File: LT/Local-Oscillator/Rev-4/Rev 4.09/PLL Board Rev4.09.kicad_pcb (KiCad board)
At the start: 2 copper layers, 109.2 x 45.7 mm, 69 parts, among them J1 Conn_01x02_Male, J13 Conn_01x02_Male, J14 Conn_01x02_Male, J15 Conn_01x02_Male, J16 Conn_01x02_Male, J17 Conn_01x02_Male, J18 Conn_Coaxial, J2 Conn_Coaxial, J20 Conn_01x02_Male, J3 Conn_Coaxial, J4 Conn_01x04_Male, J5 Conn_01x02_Male, J7 Conn_01x02_Male, J8 Conn_01x02_Male, Q1 2N5486 JFET, Q2 2N5486 JFET, U1 LMX231X, U2 L7808

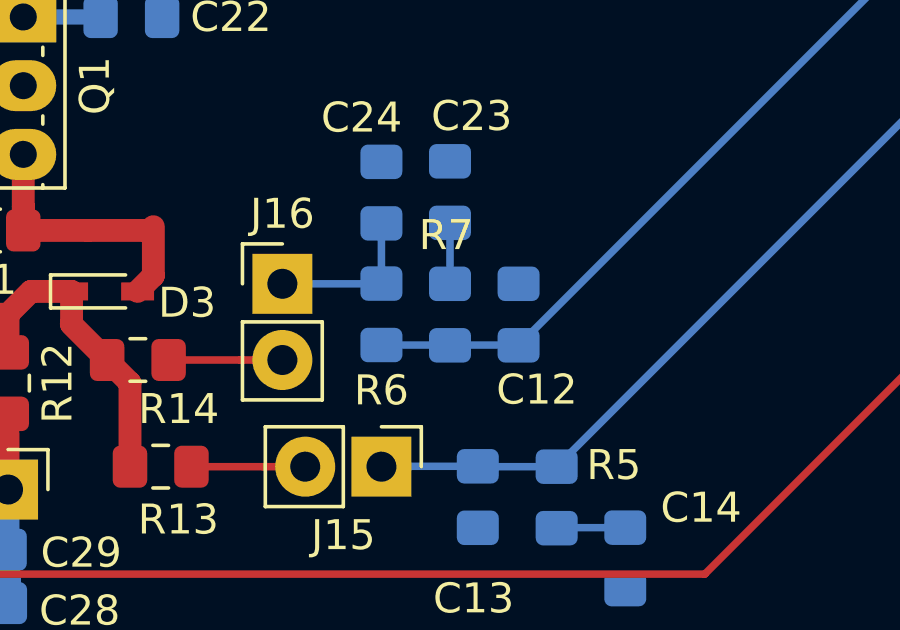
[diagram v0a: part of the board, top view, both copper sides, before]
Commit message: Finished PLL Revisions on KiCad
The KiCad files for the PLL have been uploaded to github and the integration to the "Real Resistor" symbol has begun
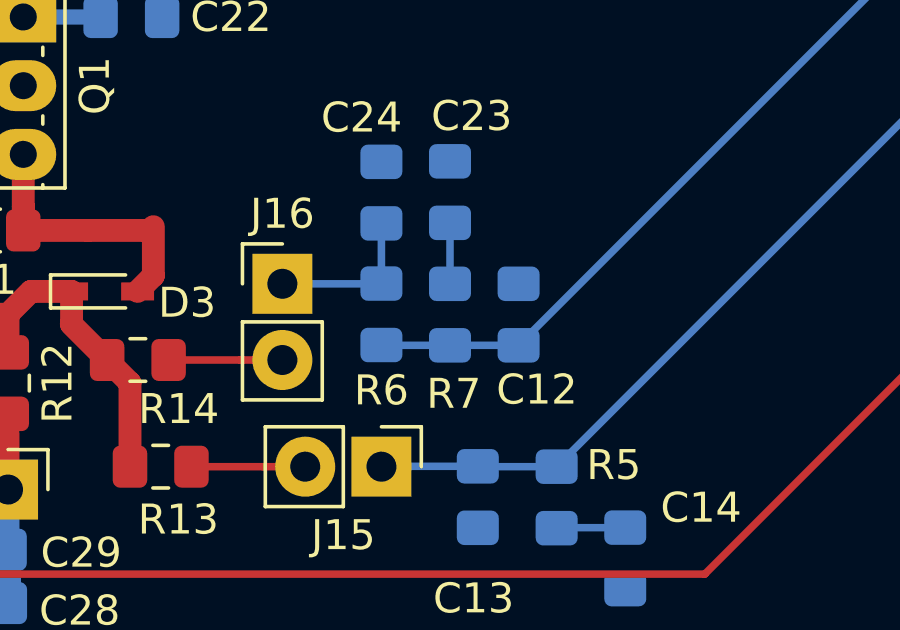
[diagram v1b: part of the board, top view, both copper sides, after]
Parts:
- C19: value TZB4Z100BA10R00 -> SGC35060
- D3, D4: value ??? -> 1SV304
- turned R7 to 90 degrees
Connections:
- R7 pad 1: Net-(C23-Pad1) -> Net-(C12-Pad2)
- R7 pad 2: Net-(C12-Pad2) -> Net-(C23-Pad1)
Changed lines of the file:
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@@
     (thickness 1.6)
     (drawings 4)
-    (tracks 248)
+    (tracks 247)
     (zones 0)
     (modules 69)
@@
       (effects (font (size 1 1) (thickness 0.15)))
     )
-    (fp_text value "TZB4Z100BA10R00 " (at 0 3.25 270) (layer F.Fab)
+    (fp_text value SGC35060 (at 0 3.25 270) (layer F.Fab)
       (effects (font (size 1 1) (thickness 0.15)))
     )
@@
   )
   (module Resistor_SMD:R_0805_2012Metric_Pad1.15x1.40mm_HandSolder (layer B.Cu)
-    (at 122.428 102.625 270)
+    (at 122.428 102.625 90)
     (descr "Resistor SMD 0805 (2012 Metric), square (rectangular) end terminal, IPC_7351 nominal with elongated pad for handsoldering. (Body size source: https://docs.google.com/spreadsheets/d/1BsfQQcO9C6DZCsRaXUlFlo91Tg2WpOkGARC1WS5S8t0/edit?usp=sharing), generated with kicad-footprint-generator")
     (tags "resistor handsolder")
@@
       (effects (font (size 0.5 0.5) (thickness 0.08)) (justify mirror))
     )
-    (pad 1 smd roundrect (at -1.025 0 270) (size 1.15 1.4) (layers B.Cu B.Paste B.Mask) (roundrect_rratio 0.217391)
-      (net 35 "Net-(C23-Pad1)"))
-    (pad 2 smd roundrect (at 1.025 0 270) (size 1.15 1.4) (layers B.Cu B.Paste B.Mask) (roundrect_rratio 0.217391)
+    (pad 1 smd roundrect (at -1.025 0 90) (size 1.15 1.4) (layers B.Cu B.Paste B.Mask) (roundrect_rratio 0.217391)
       (net 6 "Net-(C12-Pad2)"))
+    (pad 2 smd roundrect (at 1.025 0 90) (size 1.15 1.4) (layers B.Cu B.Paste B.Mask) (roundrect_rratio 0.217391)
+      (net 35 "Net-(C23-Pad1)"))
     (model ${KISYS3DMOD}/Resistor_SMD.3dshapes/R_0805_2012Metric.wrl
       (at (xyz 0 0 0))
@@
       (effects (font (size 1 1) (thickness 0.15)))
     )
-    (fp_text value ??? (at 0 1.6) (layer F.Fab)
+    (fp_text value 1SV304 (at 0 1.6) (layer F.Fab)
       (effects (font (size 1 1) (thickness 0.15)))
     )
@@
       (effects (font (size 1 1) (thickness 0.15)))
     )
-    (fp_text value ??? (at 0 1.6 270) (layer F.Fab)
+    (fp_text value 1SV304 (at 0 1.6 270) (layer F.Fab)
       (effects (font (size 1 1) (thickness 0.15)))
     )
@@
   (segment (start 141.478 90.424) (end 137.94 90.424) (width 0.25) (layer B.Cu) (net 6) (status 10))
   (segment (start 120.151 103.65) (end 120.142 103.641) (width 0.25) (layer B.Cu) (net 6) (status 30))
-  (segment (start 124.705 103.641) (end 124.714 103.65) (width 0.25) (layer B.Cu) (net 6))
-  (segment (start 120.142 103.641) (end 124.705 103.641) (width 0.25) (layer B.Cu) (net 6))
+  (segment (start 124.714 103.65) (end 120.151 103.65) (width 0.25) (layer B.Cu) (net 6) (status 30))
   (segment (start 105.918 94.996) (end 105.664 95.25) (width 0.508) (layer F.Cu) (net 7) (status 30))
   (segment (start 108.204 94.996) (end 105.918 94.996) (width 0.508) (layer F.Cu) (net 7) (status 30))
@@
   (segment (start 86.5552 97.1042) (end 86.5124 97.0614) (width 0.25) (layer F.Cu) (net 34) (status 30))
   (segment (start 89.154 97.1042) (end 86.5552 97.1042) (width 0.508) (layer F.Cu) (net 34) (status 30))
-  (segment (start 122.428 99.568) (end 122.428 101.6) (width 0.25) (layer B.Cu) (net 35))
+  (segment (start 122.428 101.6) (end 122.428 99.568) (width 0.25) (layer B.Cu) (net 35) (status 30))
   (segment (start 120.142 101.591) (end 120.142 99.586) (width 0.25) (layer B.Cu) (net 36) (status 30))
   (segment (start 120.133 101.6) (end 120.142 101.591) (width 0.25) (layer B.Cu) (net 36) (status 30))

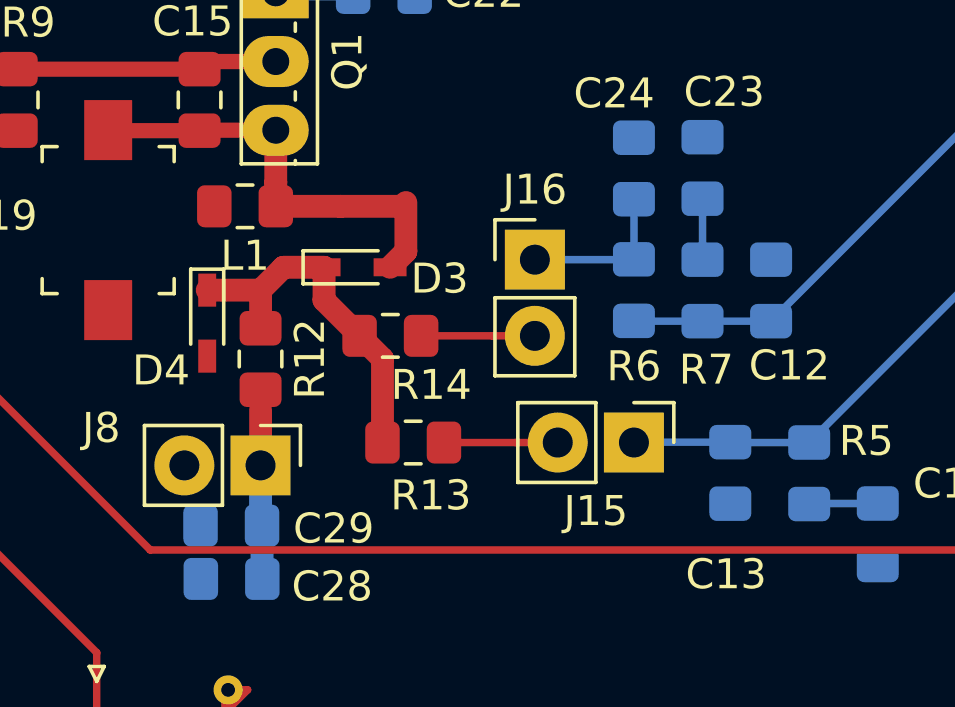
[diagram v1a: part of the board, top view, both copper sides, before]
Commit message: Finished PLL Resistor Symbols
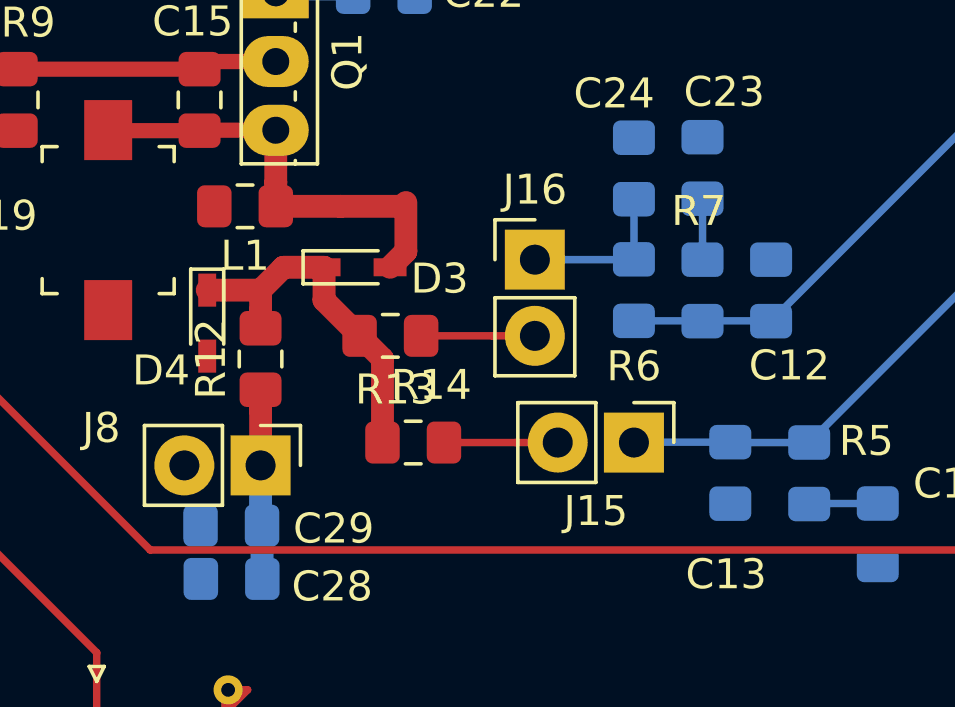
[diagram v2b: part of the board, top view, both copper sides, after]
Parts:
- R13, R14: value 0k -> 0
- turned R12 to 90 degrees
- turned R13 to 180 degrees
- turned R7 to 270 degrees
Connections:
- R12 pad 1: Net-(D3-Pad1) -> Net-(C28-Pad2)
- R12 pad 2: Net-(C28-Pad2) -> Net-(D3-Pad1)
- R13 pad 1: Net-(D3-Pad1) -> Net-(J15-Pad2)
- R13 pad 2: Net-(J15-Pad2) -> Net-(D3-Pad1)
- R7 pad 1: Net-(C12-Pad2) -> Net-(C23-Pad1)
- R7 pad 2: Net-(C23-Pad1) -> Net-(C12-Pad2)
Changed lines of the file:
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@@
     (thickness 1.6)
     (drawings 4)
-    (tracks 247)
+    (tracks 249)
     (zones 0)
     (modules 69)
@@
       (effects (font (size 1 1) (thickness 0.15)))
     )
-    (fp_text value 0k (at 0 1.65 180) (layer F.Fab)
+    (fp_text value 0 (at 0 1.65 180) (layer F.Fab)
       (effects (font (size 1 1) (thickness 0.15)))
     )
@@
   )
   (module Resistor_SMD:R_0805_2012Metric_Pad1.15x1.40mm_HandSolder (layer F.Cu)
-    (at 112.785 107.696)
+    (at 112.785 107.696 180)
     (descr "Resistor SMD 0805 (2012 Metric), square (rectangular) end terminal, IPC_7351 nominal with elongated pad for handsoldering. (Body size source: https://docs.google.com/spreadsheets/d/1BsfQQcO9C6DZCsRaXUlFlo91Tg2WpOkGARC1WS5S8t0/edit?usp=sharing), generated with kicad-footprint-generator")
     (tags "resistor handsolder")
@@
       (effects (font (size 1 1) (thickness 0.15)))
     )
-    (fp_text value 0k (at 0 1.65) (layer F.Fab)
+    (fp_text value 0 (at 0 1.65) (layer F.Fab)
       (effects (font (size 1 1) (thickness 0.15)))
     )
@@
       (effects (font (size 0.5 0.5) (thickness 0.08)))
     )
-    (pad 1 smd roundrect (at -1.025 0) (size 1.15 1.4) (layers F.Cu F.Paste F.Mask) (roundrect_rratio 0.217391)
-      (net 13 "Net-(D3-Pad1)"))
-    (pad 2 smd roundrect (at 1.025 0) (size 1.15 1.4) (layers F.Cu F.Paste F.Mask) (roundrect_rratio 0.217391)
+    (pad 1 smd roundrect (at -1.025 0 180) (size 1.15 1.4) (layers F.Cu F.Paste F.Mask) (roundrect_rratio 0.217391)
       (net 37 "Net-(J15-Pad2)"))
+    (pad 2 smd roundrect (at 1.025 0 180) (size 1.15 1.4) (layers F.Cu F.Paste F.Mask) (roundrect_rratio 0.217391)
+      (net 13 "Net-(D3-Pad1)"))
     (model ${KISYS3DMOD}/Resistor_SMD.3dshapes/R_0805_2012Metric.wrl
       (at (xyz 0 0 0))
@@
   )
   (module Resistor_SMD:R_0805_2012Metric_Pad1.15x1.40mm_HandSolder (layer F.Cu)
-    (at 107.696 104.911 270)
+    (at 107.696 104.911 90)
     (descr "Resistor SMD 0805 (2012 Metric), square (rectangular) end terminal, IPC_7351 nominal with elongated pad for handsoldering. (Body size source: https://docs.google.com/spreadsheets/d/1BsfQQcO9C6DZCsRaXUlFlo91Tg2WpOkGARC1WS5S8t0/edit?usp=sharing), generated with kicad-footprint-generator")
     (tags "resistor handsolder")
@@
       (effects (font (size 0.5 0.5) (thickness 0.08)))
     )
-    (pad 1 smd roundrect (at -1.025 0 270) (size 1.15 1.4) (layers F.Cu F.Paste F.Mask) (roundrect_rratio 0.217391)
-      (net 13 "Net-(D3-Pad1)"))
-    (pad 2 smd roundrect (at 1.025 0 270) (size 1.15 1.4) (layers F.Cu F.Paste F.Mask) (roundrect_rratio 0.217391)
+    (pad 1 smd roundrect (at -1.025 0 90) (size 1.15 1.4) (layers F.Cu F.Paste F.Mask) (roundrect_rratio 0.217391)
       (net 39 "Net-(C28-Pad2)"))
+    (pad 2 smd roundrect (at 1.025 0 90) (size 1.15 1.4) (layers F.Cu F.Paste F.Mask) (roundrect_rratio 0.217391)
+      (net 13 "Net-(D3-Pad1)"))
     (model ${KISYS3DMOD}/Resistor_SMD.3dshapes/R_0805_2012Metric.wrl
       (at (xyz 0 0 0))
@@
   )
   (module Resistor_SMD:R_0805_2012Metric_Pad1.15x1.40mm_HandSolder (layer B.Cu)
-    (at 122.428 102.625 90)
+    (at 122.428 102.625 270)
     (descr "Resistor SMD 0805 (2012 Metric), square (rectangular) end terminal, IPC_7351 nominal with elongated pad for handsoldering. (Body size source: https://docs.google.com/spreadsheets/d/1BsfQQcO9C6DZCsRaXUlFlo91Tg2WpOkGARC1WS5S8t0/edit?usp=sharing), generated with kicad-footprint-generator")
     (tags "resistor handsolder")
@@
       (effects (font (size 0.5 0.5) (thickness 0.08)) (justify mirror))
     )
-    (pad 1 smd roundrect (at -1.025 0 90) (size 1.15 1.4) (layers B.Cu B.Paste B.Mask) (roundrect_rratio 0.217391)
-      (net 6 "Net-(C12-Pad2)"))
-    (pad 2 smd roundrect (at 1.025 0 90) (size 1.15 1.4) (layers B.Cu B.Paste B.Mask) (roundrect_rratio 0.217391)
+    (pad 1 smd roundrect (at -1.025 0 270) (size 1.15 1.4) (layers B.Cu B.Paste B.Mask) (roundrect_rratio 0.217391)
       (net 35 "Net-(C23-Pad1)"))
+    (pad 2 smd roundrect (at 1.025 0 270) (size 1.15 1.4) (layers B.Cu B.Paste B.Mask) (roundrect_rratio 0.217391)
+      (net 6 "Net-(C12-Pad2)"))
     (model ${KISYS3DMOD}/Resistor_SMD.3dshapes/R_0805_2012Metric.wrl
       (at (xyz 0 0 0))
@@
   (segment (start 141.478 90.424) (end 137.94 90.424) (width 0.25) (layer B.Cu) (net 6) (status 10))
   (segment (start 120.151 103.65) (end 120.142 103.641) (width 0.25) (layer B.Cu) (net 6) (status 30))
-  (segment (start 124.714 103.65) (end 120.151 103.65) (width 0.25) (layer B.Cu) (net 6) (status 30))
+  (segment (start 124.705 103.641) (end 124.714 103.65) (width 0.25) (layer B.Cu) (net 6))
+  (segment (start 120.142 103.641) (end 124.705 103.641) (width 0.25) (layer B.Cu) (net 6))
   (segment (start 105.918 94.996) (end 105.664 95.25) (width 0.508) (layer F.Cu) (net 7) (status 30))
   (segment (start 108.204 94.996) (end 105.918 94.996) (width 0.508) (layer F.Cu) (net 7) (status 30))
@@
   (segment (start 184.8358 87.9856) (end 184.8358 93.6498) (width 0.762) (layer F.Cu) (net 12) (status 30))
   (segment (start 111.76 104.902) (end 110.998 104.14) (width 0.762) (layer F.Cu) (net 13) (status 20))
-  (segment (start 111.76 107.696) (end 111.76 104.902) (width 0.762) (layer F.Cu) (net 13) (status 10))
   (segment (start 110.064 101.854) (end 109.814 101.854) (width 0.25) (layer F.Cu) (net 13) (status 30))
   (segment (start 105.918 102.366) (end 105.918 102.616) (width 0.25) (layer F.Cu) (net 13) (status 30))
   (segment (start 109.728 101.854) (end 109.814 101.854) (width 0.25) (layer F.Cu) (net 13) (status 30))
   (segment (start 106.468 102.616) (end 105.918 102.616) (width 0.762) (layer F.Cu) (net 13) (status 20))
-  (segment (start 107.696 103.886) (end 107.696 102.616) (width 0.762) (layer F.Cu) (net 13) (status 10))
   (segment (start 107.696 102.616) (end 106.468 102.616) (width 0.762) (layer F.Cu) (net 13))
   (segment (start 108.458 101.854) (end 109.814 101.854) (width 0.762) (layer F.Cu) (net 13) (status 20))
@@
   (segment (start 109.814 102.9364) (end 109.814 101.854) (width 0.762) (layer F.Cu) (net 13) (status 20))
   (segment (start 109.8042 102.9462) (end 109.814 102.9364) (width 0.25) (layer F.Cu) (net 13))
+  (segment (start 111.76 104.902) (end 111.76 107.696) (width 0.762) (layer F.Cu) (net 13))
+  (segment (start 107.696 103.311) (end 107.696 102.616) (width 0.762) (layer F.Cu) (net 13))
+  (segment (start 107.696 103.886) (end 107.696 103.311) (width 0.762) (layer F.Cu) (net 13))
   (segment (start 114.663787 87.376) (end 112.268 87.376) (width 0.508) (layer B.Cu) (net 14) (status 20))
   (segment (start 116.078 87.376) (end 114.663787 87.376) (width 0.508) (layer B.Cu) (net 14) (status 10))
@@
   (segment (start 86.5552 97.1042) (end 86.5124 97.0614) (width 0.25) (layer F.Cu) (net 34) (status 30))
   (segment (start 89.154 97.1042) (end 86.5552 97.1042) (width 0.508) (layer F.Cu) (net 34) (status 30))
-  (segment (start 122.428 101.6) (end 122.428 99.568) (width 0.25) (layer B.Cu) (net 35) (status 30))
+  (segment (start 122.428 99.568) (end 122.428 101.6) (width 0.25) (layer B.Cu) (net 35))
   (segment (start 120.142 101.591) (end 120.142 99.586) (width 0.25) (layer B.Cu) (net 36) (status 30))
   (segment (start 120.133 101.6) (end 120.142 101.591) (width 0.25) (layer B.Cu) (net 36) (status 30))
   (segment (start 116.84 101.6) (end 120.133 101.6) (width 0.25) (layer B.Cu) (net 36) (status 30))
-  (segment (start 116.187787 107.696) (end 113.81 107.696) (width 0.25) (layer F.Cu) (net 37) (status 20))
   (segment (start 117.602 107.696) (end 116.187787 107.696) (width 0.25) (layer F.Cu) (net 37) (status 10))
+  (segment (start 113.81 107.696) (end 116.187787 107.696) (width 0.25) (layer F.Cu) (net 37))
   (segment (start 115.425787 104.14) (end 113.048 104.14) (width 0.25) (layer F.Cu) (net 38) (status 20))
   (segment (start 116.84 104.14) (end 115.425787 104.14) (width 0.25) (layer F.Cu) (net 38) (status 10))
   (segment (start 107.696 106.611) (end 107.696 108.458) (width 0.762) (layer F.Cu) (net 39) (status 20))
-  (segment (start 107.696 105.936) (end 107.696 106.611) (width 0.25) (layer F.Cu) (net 39) (status 10))
   (segment (start 107.696 110.4138) (end 107.7468 110.4646) (width 0.25) (layer B.Cu) (net 39) (status 30))
   (segment (start 107.696 108.458) (end 107.696 110.4138) (width 0.762) (layer B.Cu) (net 39) (status 30))
   (segment (start 107.7468 112.2336) (end 107.7558 112.2426) (width 0.25) (layer B.Cu) (net 39) (status 30))
   (segment (start 107.7468 110.4646) (end 107.7468 112.2336) (width 0.762) (layer B.Cu) (net 39) (status 30))
+  (segment (start 107.696 106.611) (end 107.696 105.936) (width 0.762) (layer F.Cu) (net 39))
   (zone (net 1) (net_name GND) (layer F.Cu) (hatch edge 0.508)
     (connect_pads (clearance 0.508))

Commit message: Nothing much I don't think
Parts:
- D1: footprint Diode_THT:D_DO-41_SOD81_P10.16mm_Horizontal -> Diode_SMD:D_SOD-323_HandSoldering
- moved D1 4.86 mm to (180.0, 88.0)
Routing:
- net PLL_Power: track 41.6 -> 45.7 mm
- net Net-(D1-Pad1): track 5.95 -> 9.58 mm
